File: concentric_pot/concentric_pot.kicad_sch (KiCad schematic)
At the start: 2 parts, among them J1 Dual Pot

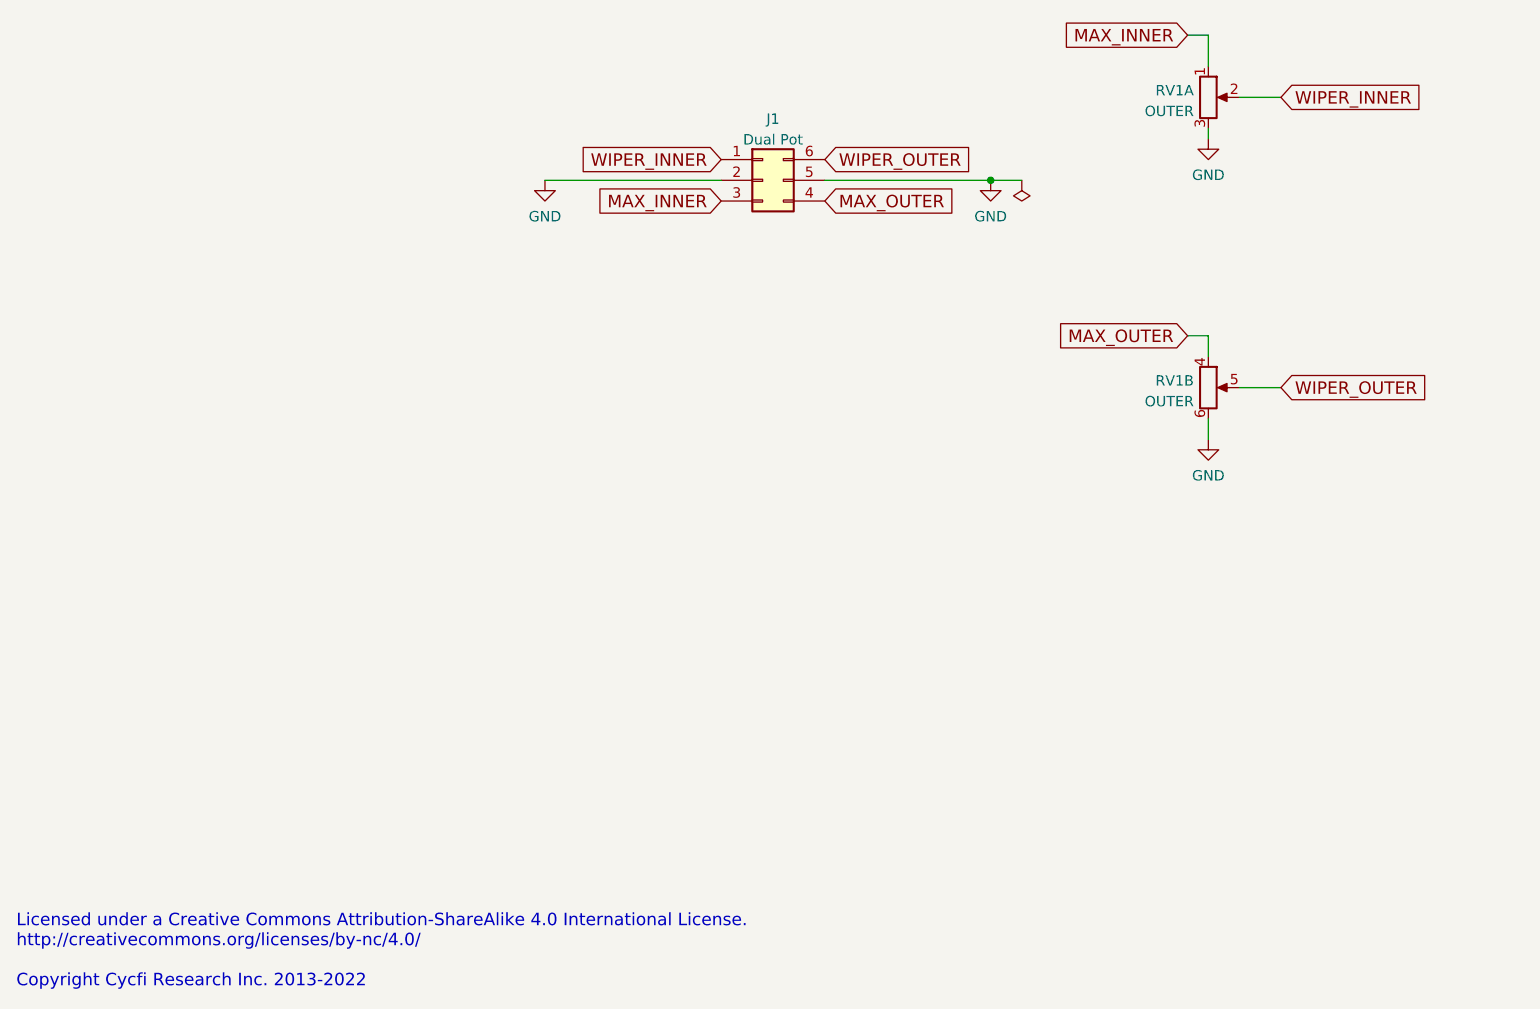
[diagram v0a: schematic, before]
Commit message: Added taper resistor
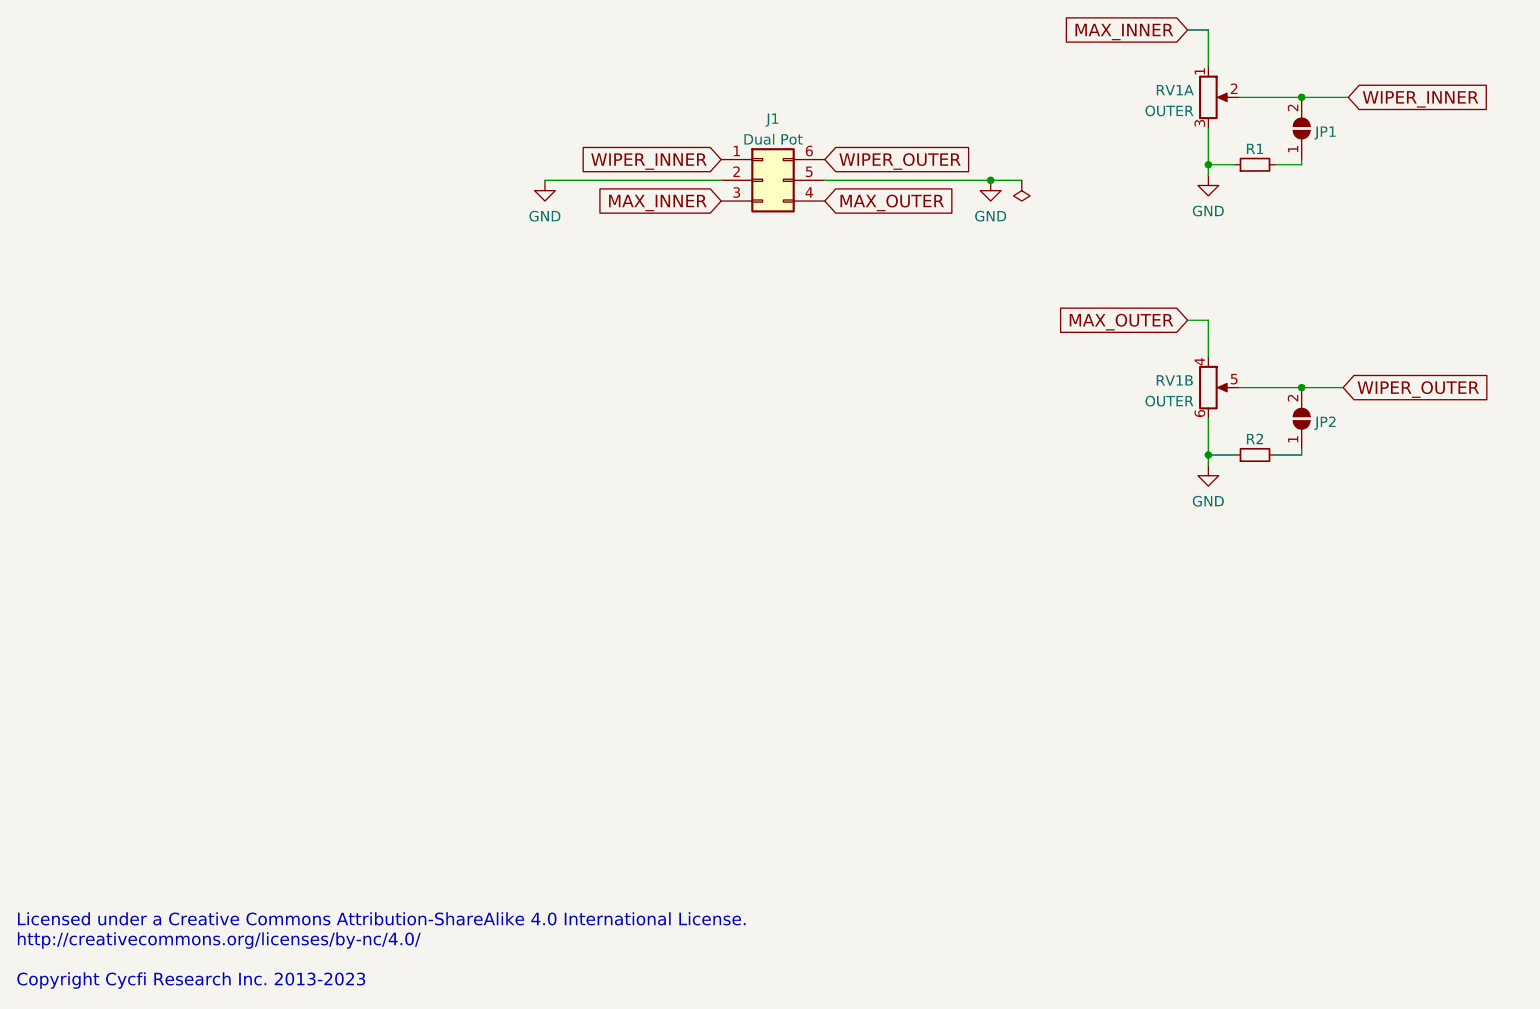
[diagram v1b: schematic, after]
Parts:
- added JP1, JP2: SolderJumper_2_Open, Jumper:SolderJumper-2_P1.3mm_Open_TrianglePad1.0x1.5mm, symbol Jumper:SolderJumper_2_Open
- added R1, R2: R_Small, Resistor_SMD:R_0805_2012Metric_Pad1.20x1.40mm_HandSolder, symbol Device:R_Small
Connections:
- net GND: now also R1.1, R2.1
- net WIPER_INNER: now also JP1.2 (B)
- net WIPER_OUTER: now also JP2.2 (B)
- new net: JP1.1 (A), R1.2
- new net: JP2.1 (A), R2.2
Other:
- note added: "Licensed under a Creative Commons Attribution-ShareAlike 4.0 International License. http://creativecommons.org/licenses/by-nc/4.0/ Copyright Cycfi Research Inc. 2013-2023"
- note removed: "Licensed under a Creative Commons Attribution-ShareAlike 4.0 International License. http://creativecommons.org/licenses/by-nc/4.0/ Copyright Cycfi Research Inc. 2013-2022"

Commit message: Update to v3.1
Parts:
- R1, R2: LCSC (none) -> C17673
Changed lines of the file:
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@@
       (effects (font (size 1.27 1.27)) hide)
+    )
+    (property "LCSC" "C17673" (id 4) (at 175.895 122.555 90)
+      (effects (font (size 1.524 1.524)) hide)
     )
     (pin "1")
@@
       (effects (font (size 1.27 1.27)) hide)
     )
+    (property "LCSC" "C17673" (id 4) (at 175.895 86.995 90)
+      (effects (font (size 1.524 1.524)) hide)
+    )
     (pin "1")
